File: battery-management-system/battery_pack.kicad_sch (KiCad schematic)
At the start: 15 parts

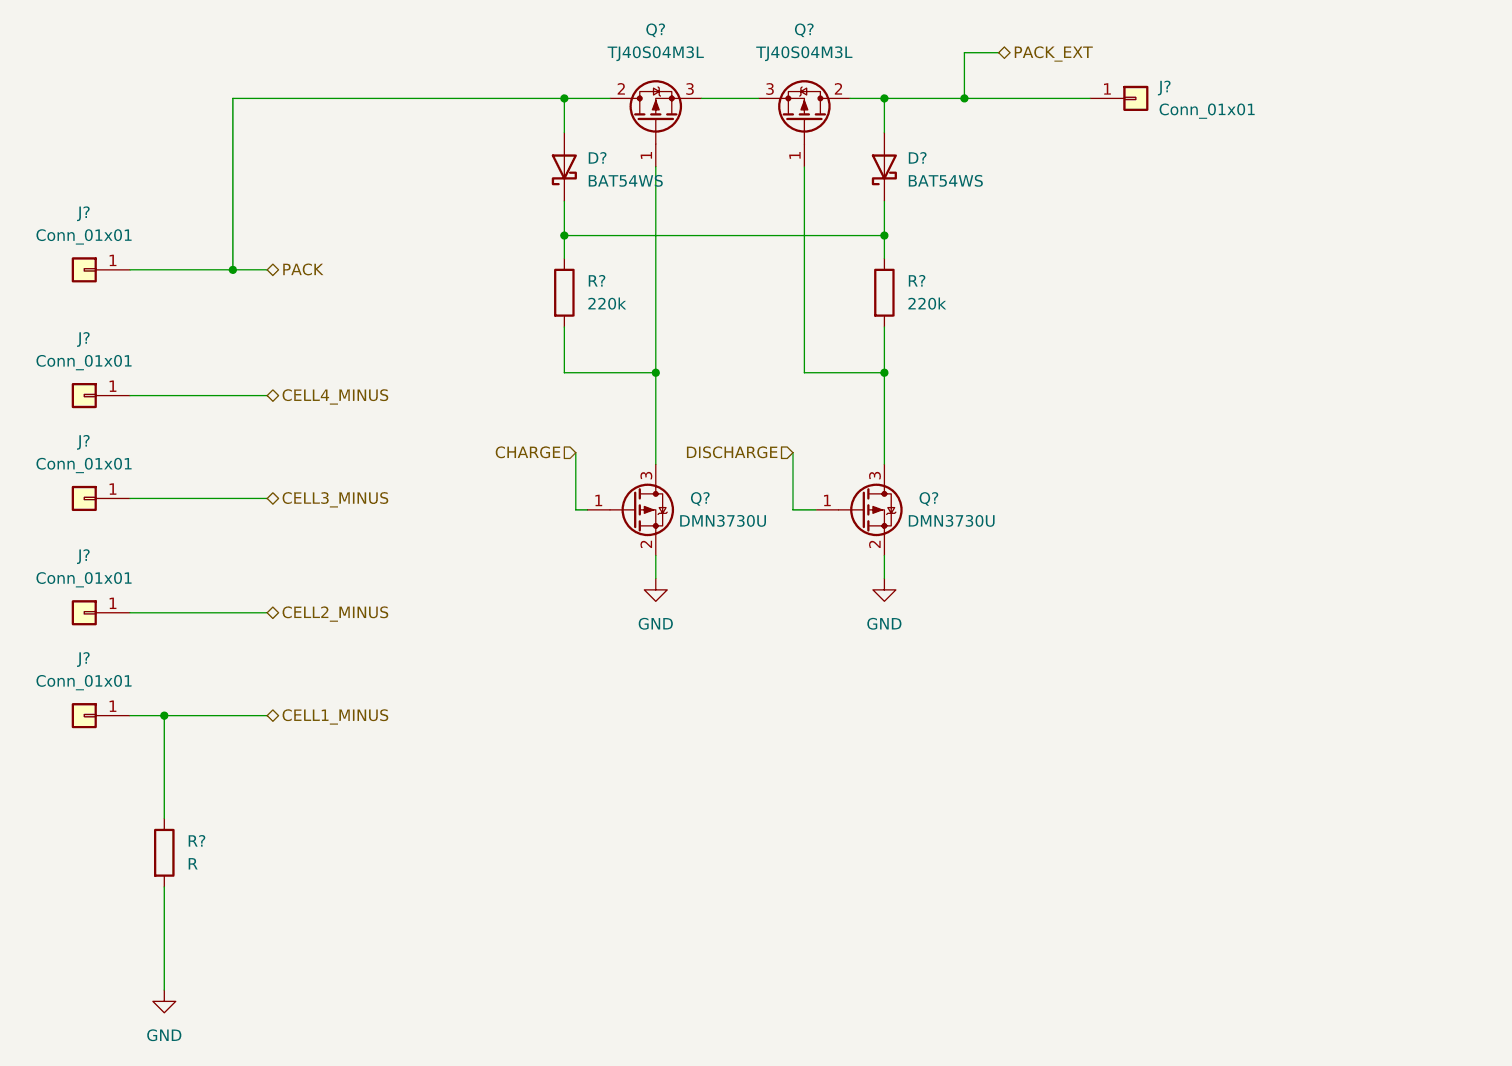
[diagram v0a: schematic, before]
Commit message: add RS order numbers
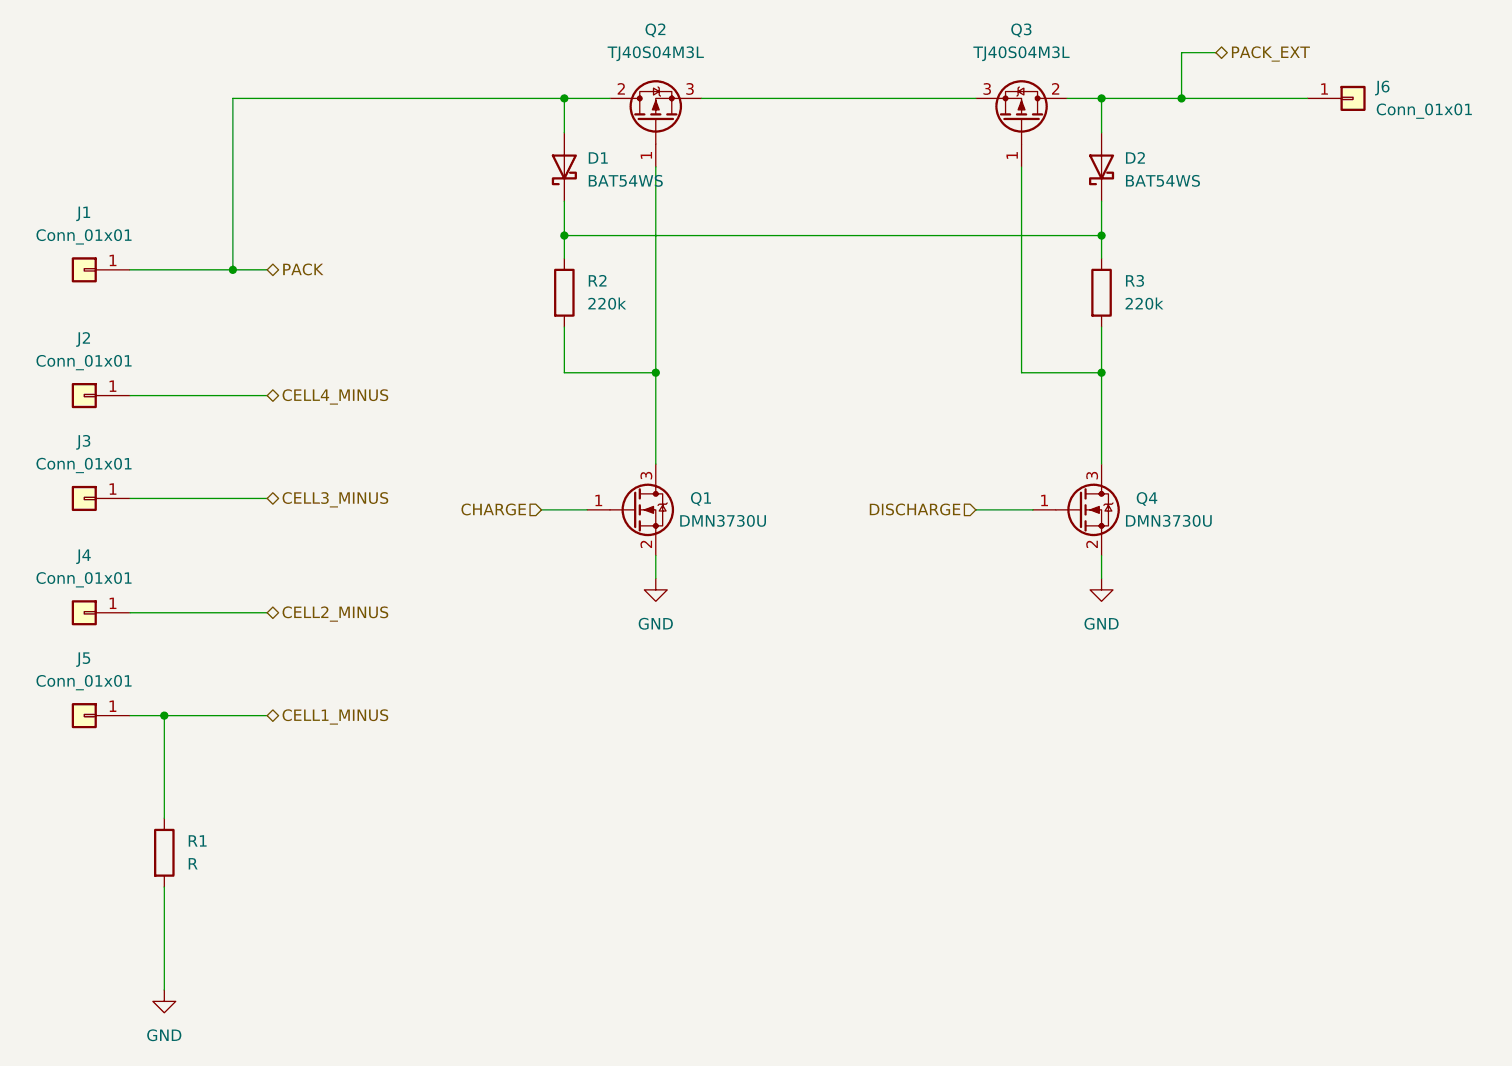
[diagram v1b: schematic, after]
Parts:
- removed D?: BAT54WS, Diode_SMD:D_SOD-323, symbol benediktibk:BAT54WS
- added D1: BAT54WS, Diode_SMD:D_SOD-323, symbol benediktibk:BAT54WS
- D2: renamed from D?; RS order number (none) -> 738-4844
- Q1, Q4: renamed from Q?; RS order number (none) -> 823-2946
- Q2, Q3: renamed from Q?; RS order number (none) -> 171-2479
- gave numbers to parts that had none: 9
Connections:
- net PACK: now also D1.2 (A)
- net at D2.1 (K), R2.1, R3.1: now also D1.1 (K)
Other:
- moved on the sheet: D2, J6, Q3, Q4, R3

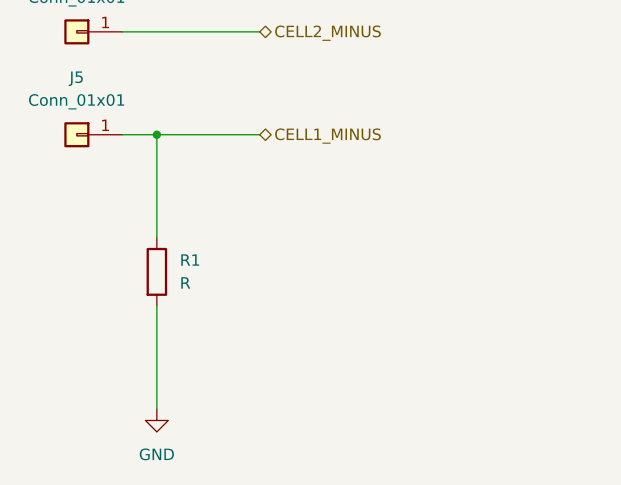
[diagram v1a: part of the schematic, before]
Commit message: define current sense resistance value
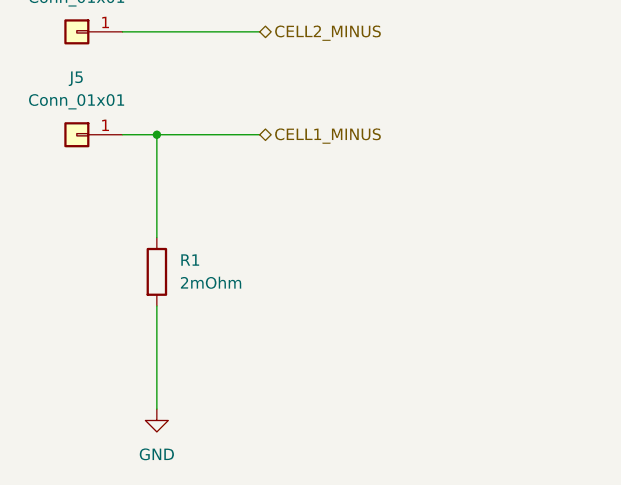
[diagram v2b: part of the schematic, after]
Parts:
- R1: value R -> 2mOhm
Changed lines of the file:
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@@
       (effects (font (size 1.27 1.27)) (justify left))
     )
-    (property "Value" "R" (id 1) (at 77.47 130.8099 0)
+    (property "Value" "2mOhm" (id 1) (at 77.47 130.8099 0)
       (effects (font (size 1.27 1.27)) (justify left))
     )

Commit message: use own symbols and footprints
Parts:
- D1, D2: footprint Diode_SMD:D_SOD-323 -> benediktibk:D_SOD-323
- Q1, Q4: footprint Package_TO_SOT_SMD:SOT-23 -> benediktibk:SOT-23
- Q2, Q3: footprint Package_TO_SOT_SMD:TO-252-2 -> benediktibk:TO-252-2
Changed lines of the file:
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@@
       (effects (font (size 1.27 1.27)) (justify right))
     )
-    (property "Footprint" "Diode_SMD:D_SOD-323" (id 2) (at 119.38 53.34 0)
+    (property "Footprint" "benediktibk:D_SOD-323" (id 2) (at 119.38 53.34 0)
       (effects (font (size 1.27 1.27)) hide)
     )
@@
     (property "Reference" "Q3" (id 0) (at 170.18 38.1 90))
     (property "Value" "TJ40S04M3L" (id 1) (at 170.18 40.64 90))
-    (property "Footprint" "Package_TO_SOT_SMD:TO-252-2" (id 2) (at 172.72 43.18 0)
+    (property "Footprint" "benediktibk:TO-252-2" (id 2) (at 172.72 43.18 0)
       (effects (font (size 1.27 1.27)) hide)
     )
@@
     (property "Reference" "Q2" (id 0) (at 129.54 38.1 90))
     (property "Value" "TJ40S04M3L" (id 1) (at 129.54 40.64 90))
-    (property "Footprint" "Package_TO_SOT_SMD:TO-252-2" (id 2) (at 127 43.18 0)
+    (property "Footprint" "benediktibk:TO-252-2" (id 2) (at 127 43.18 0)
       (effects (font (size 1.27 1.27)) hide)
     )
@@
     (pin "2")
   )
-  (symbol (lib_name "DMN3730U_1") (lib_id "benediktibk:DMN3730U") (at 176.53 91.44 0) (unit 1)
+  (symbol (lib_id "benediktibk:DMN3730U") (at 176.53 91.44 0) (unit 1)
     (in_bom yes) (on_board yes) (fields_autoplaced)
     (property "Reference" "Q4" (id 0) (at 182.88 90.1699 0)
@@
       (effects (font (size 1.27 1.27)) (justify left))
     )
-    (property "Footprint" "Package_TO_SOT_SMD:SOT-23" (id 2) (at 181.61 88.9 0)
+    (property "Footprint" "benediktibk:SOT-23" (id 2) (at 181.61 88.9 0)
       (effects (font (size 1.27 1.27)) hide)
     )
@@
       (effects (font (size 1.27 1.27)) (justify left))
     )
-    (property "Footprint" "Package_TO_SOT_SMD:SOT-23" (id 2) (at 132.08 88.9 0)
+    (property "Footprint" "benediktibk:SOT-23" (id 2) (at 132.08 88.9 0)
       (effects (font (size 1.27 1.27)) hide)
     )
@@
     (pin "1")
   )
-  (symbol (lib_id "benediktibk:BAT54WS") (at 179.07 53.34 90) (unit 1)
+  (symbol (lib_name "BAT54WS_1") (lib_id "benediktibk:BAT54WS") (at 179.07 53.34 90) (unit 1)
     (in_bom yes) (on_board yes) (fields_autoplaced)
     (property "Reference" "D2" (id 0) (at 181.61 52.3874 90)
@@
       (effects (font (size 1.27 1.27)) (justify right))
     )
-    (property "Footprint" "Diode_SMD:D_SOD-323" (id 2) (at 179.07 53.34 0)
-      (effects (font (size 1.27 1.27)) hide)
-    )
+    (property "Footprint" "benediktibk:D_SOD-323" (id 2) (at 179.07 53.34 0)
+      (effects (font (size 1.27 1.27)) hide)
+    )

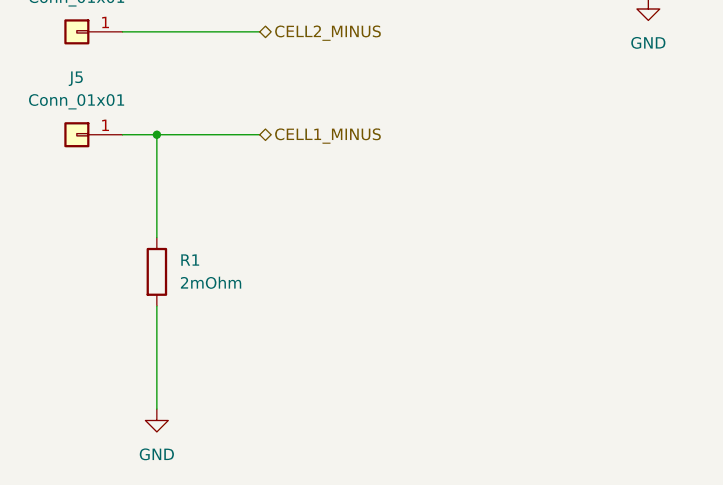
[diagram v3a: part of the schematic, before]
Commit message: use correct symbol for current sense resistor
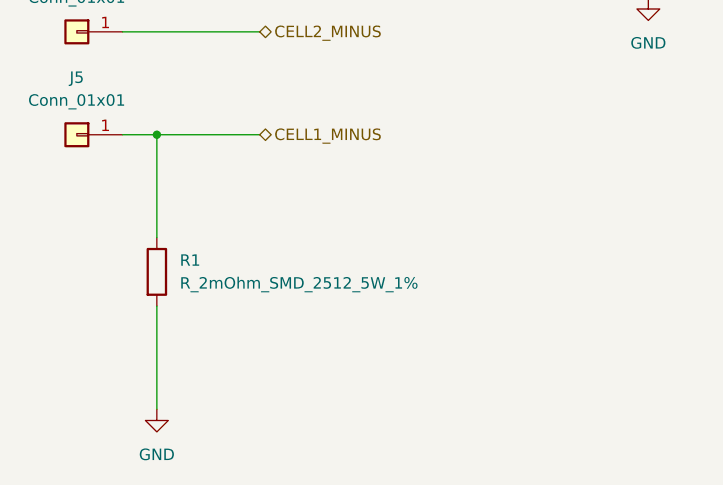
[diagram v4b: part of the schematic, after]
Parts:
- R1: value 2mOhm -> R_2mOhm_SMD_2512_5W_1%; footprint (none) -> benediktibk:R_2512_6332Metric_Pad1.40x3.35mm_HandSolder; symbol Device:R -> benediktibk:R_2mOhm_SMD_2512_5W_1%; RS order number (none) -> 231-3683
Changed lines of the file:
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@@
     (pin "3")
   )
-  (symbol (lib_id "Device:R") (at 74.93 129.54 0) (unit 1)
+  (symbol (lib_id "benediktibk:R_2mOhm_SMD_2512_5W_1%") (at 74.93 129.54 0) (unit 1)
     (in_bom yes) (on_board yes) (fields_autoplaced)
     (property "Reference" "R1" (id 0) (at 77.47 128.2699 0)
       (effects (font (size 1.27 1.27)) (justify left))
     )
-    (property "Value" "2mOhm" (id 1) (at 77.47 130.8099 0)
+    (property "Value" "R_2mOhm_SMD_2512_5W_1%" (id 1) (at 77.47 130.8099 0)
       (effects (font (size 1.27 1.27)) (justify left))
     )
-    (property "Footprint" "" (id 2) (at 73.152 129.54 90)
+    (property "Footprint" "benediktibk:R_2512_6332Metric_Pad1.40x3.35mm_HandSolder" (id 2) (at 64.77 129.032 90)
       (effects (font (size 1.27 1.27)) hide)
     )
@@
       (effects (font (size 1.27 1.27)) hide)
     )
+    (property "RS order number" "    231-3683" (id 4) (at 57.15 128.27 0)
+      (effects (font (size 1.27 1.27)) hide)
+    )

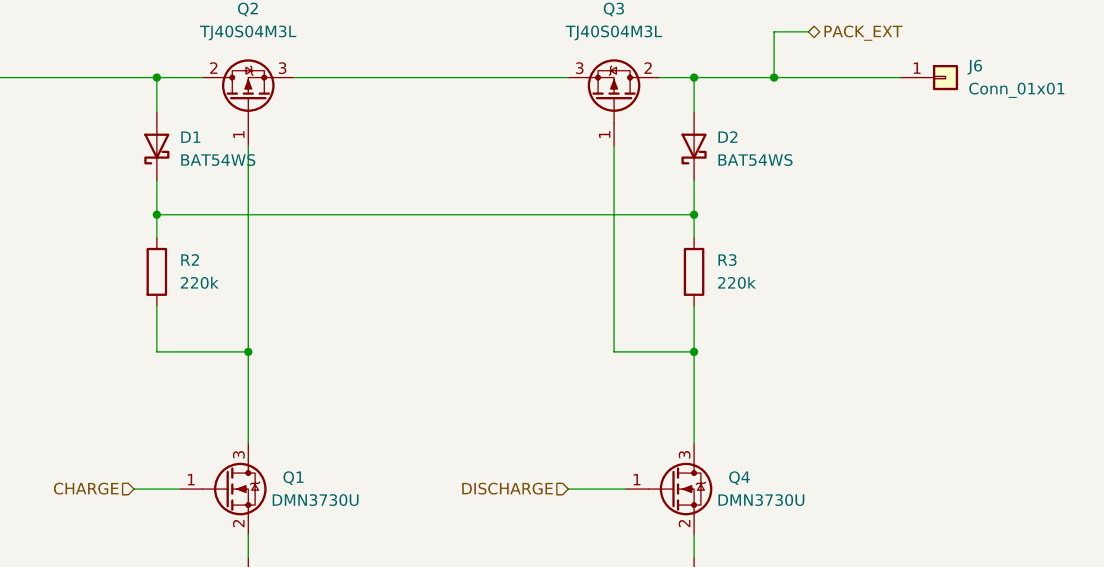
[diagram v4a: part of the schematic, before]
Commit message: specify footprints for resistors, capacitors and inductances
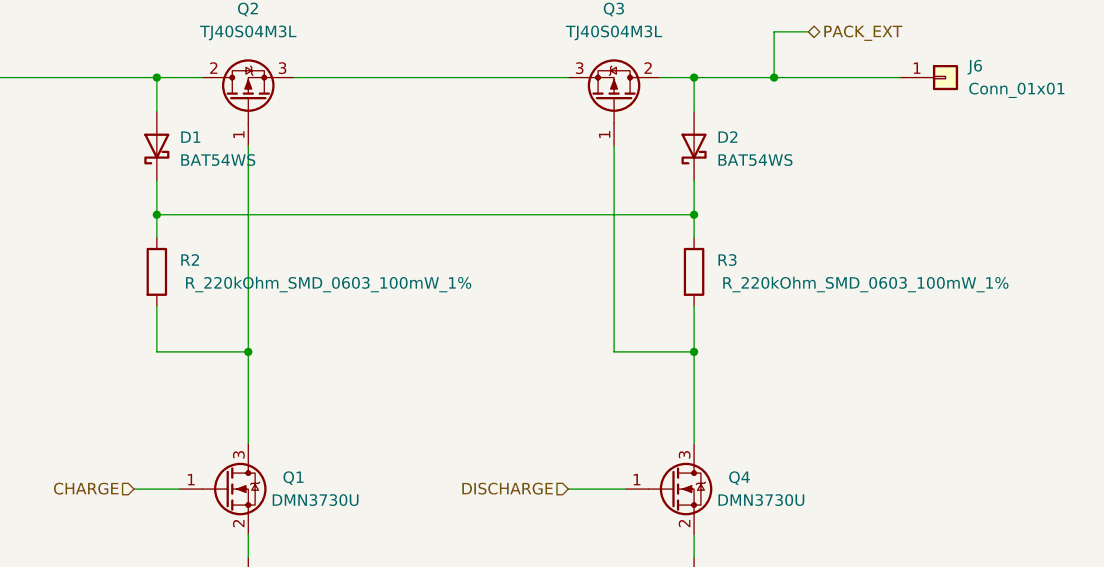
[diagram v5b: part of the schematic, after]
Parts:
- R2, R3: value 220k -> R_220kOhm_SMD_0603_100mW_1%; footprint Resistor_SMD:R_0603_1608Metric -> benediktibk:R_0603_1608Metric_Pad0.98x0.95mm_HandSolder; symbol Device:R -> benediktibk:R_220kOhm_SMD_0603_100mW_1%; RS order number (none) -> 678-9986
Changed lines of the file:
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@@
     (pin "1")
   )
-  (symbol (lib_id "Device:R") (at 119.38 67.31 0) (unit 1)
-    (in_bom yes) (on_board yes) (fields_autoplaced)
+  (symbol (lib_id "benediktibk:R_220kOhm_SMD_0603_100mW_1%") (at 119.38 67.31 0) (unit 1)
+    (in_bom yes) (on_board yes)
     (property "Reference" "R2" (id 0) (at 121.92 66.0399 0)
       (effects (font (size 1.27 1.27)) (justify left))
     )
-    (property "Value" "220k" (id 1) (at 121.92 68.5799 0)
-      (effects (font (size 1.27 1.27)) (justify left))
-    )
-    (property "Footprint" "Resistor_SMD:R_0603_1608Metric" (id 2) (at 117.602 67.31 90)
+    (property "Value" "R_220kOhm_SMD_0603_100mW_1%" (id 1) (at 138.43 68.58 0))
+    (property "Footprint" "benediktibk:R_0603_1608Metric_Pad0.98x0.95mm_HandSolder" (id 2) (at 109.22 66.802 90)
       (effects (font (size 1.27 1.27)) hide)
     )
     (property "Datasheet" "~" (id 3) (at 119.38 67.31 0)
+      (effects (font (size 1.27 1.27)) hide)
+    )
+    (property "RS order number" "678-9986" (id 4) (at 101.6 66.04 0)
       (effects (font (size 1.27 1.27)) hide)
     )
@@
     (pin "3")
   )
-  (symbol (lib_id "Device:R") (at 179.07 67.31 0) (unit 1)
-    (in_bom yes) (on_board yes) (fields_autoplaced)
+  (symbol (lib_name "R_220kOhm_SMD_0603_100mW_1%_1") (lib_id "benediktibk:R_220kOhm_SMD_0603_100mW_1%") (at 179.07 67.31 0) (unit 1)
+    (in_bom yes) (on_board yes)
     (property "Reference" "R3" (id 0) (at 181.61 66.0399 0)
       (effects (font (size 1.27 1.27)) (justify left))
     )
-    (property "Value" "220k" (id 1) (at 181.61 68.5799 0)
-      (effects (font (size 1.27 1.27)) (justify left))
-    )
-    (property "Footprint" "Resistor_SMD:R_0603_1608Metric" (id 2) (at 177.292 67.31 90)
+    (property "Value" "R_220kOhm_SMD_0603_100mW_1%" (id 1) (at 198.12 68.58 0))
+    (property "Footprint" "benediktibk:R_0603_1608Metric_Pad0.98x0.95mm_HandSolder" (id 2) (at 168.91 66.802 90)
       (effects (font (size 1.27 1.27)) hide)
     )
@@
       (effects (font (size 1.27 1.27)) hide)
     )
+    (property "RS order number" "678-9986" (id 4) (at 161.29 66.04 0)
+      (effects (font (size 1.27 1.27)) hide)
+    )
